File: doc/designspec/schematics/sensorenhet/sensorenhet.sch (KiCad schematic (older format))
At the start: 28 parts, among them IC1 ATMEGA1284P-P, U1 IQEXO-3, U10 MLX90609, U2 Terminator-CTRL, U3 USB-UART, U4 Lidar_Lite_v2, U5 IR-Sensor, U6 IR-Sensor, U7 IR-Sensor, U8 IR-Sensor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

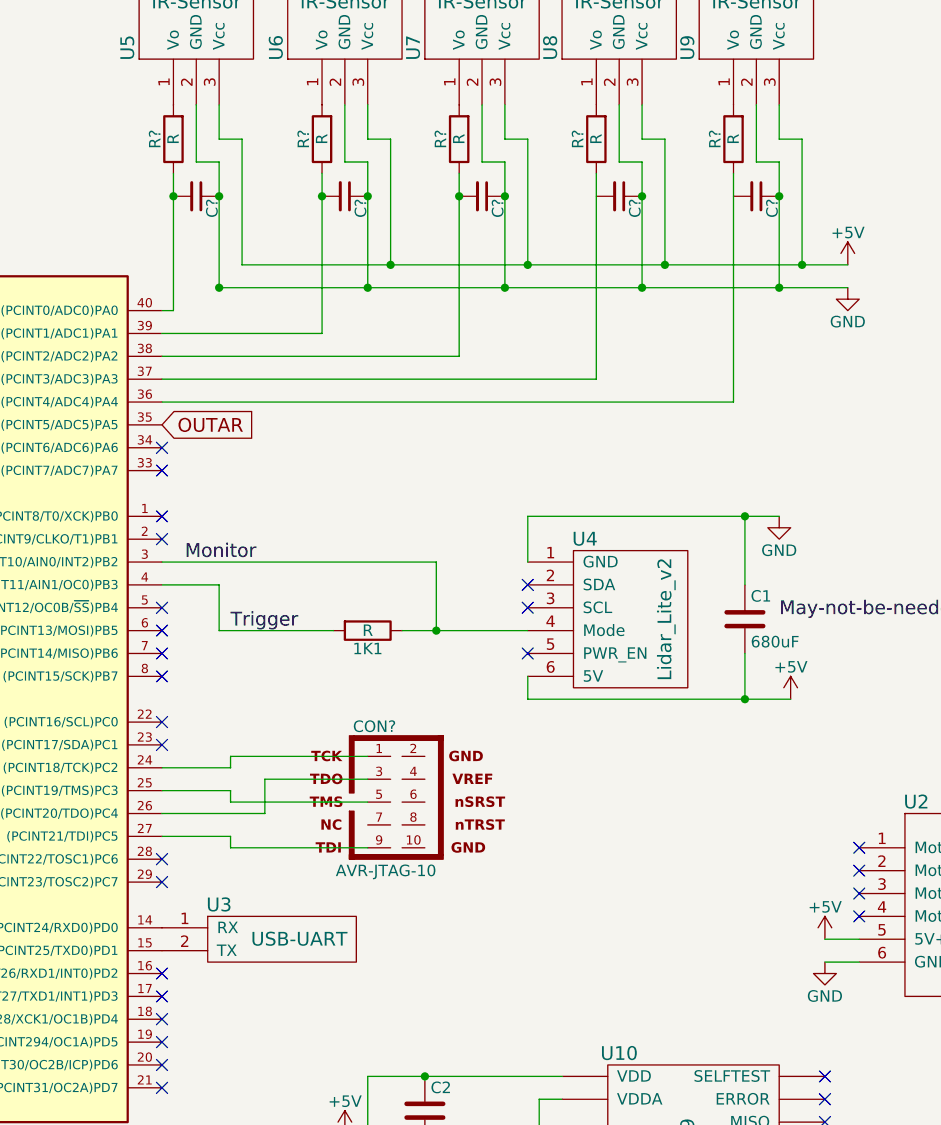
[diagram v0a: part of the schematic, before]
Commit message: Fix uart connection in kicad
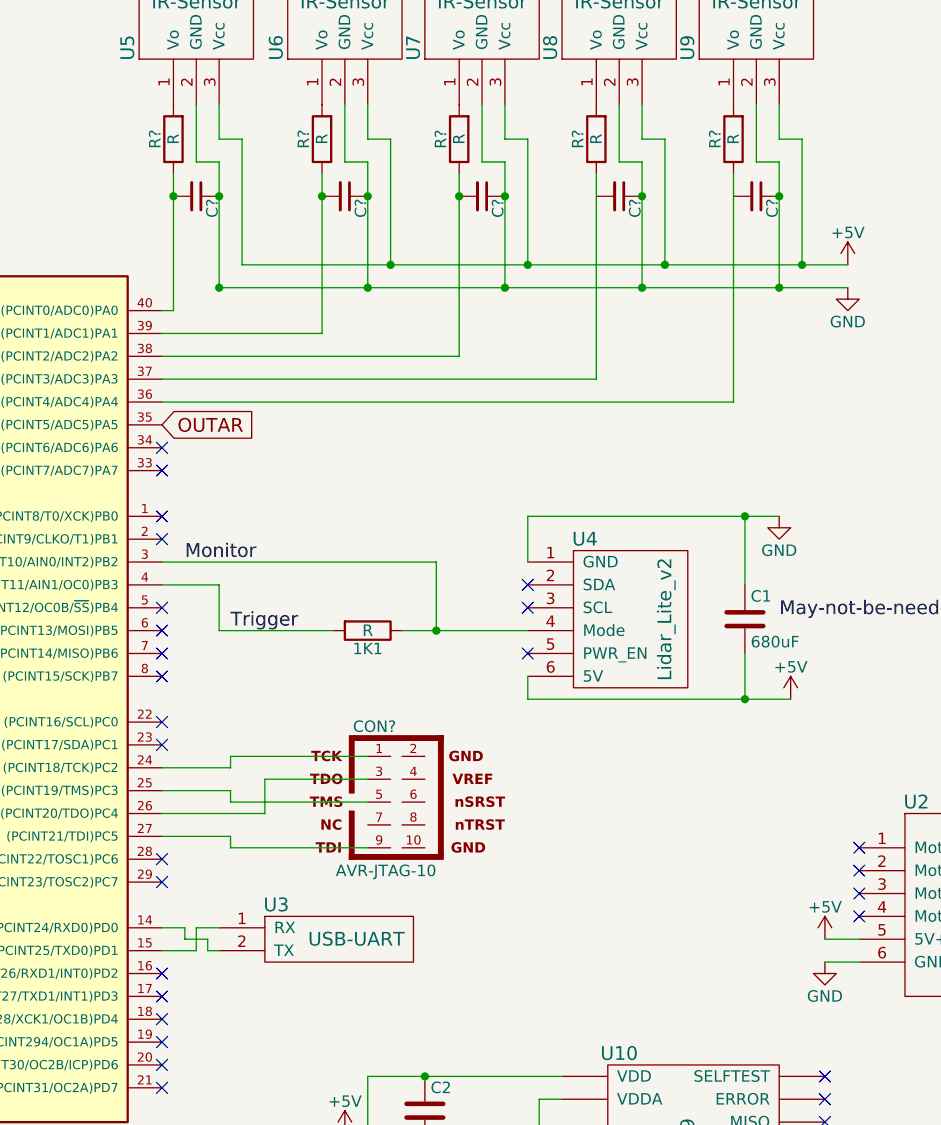
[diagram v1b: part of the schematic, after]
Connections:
- net at IC1.14 ((PCINT24/RXD0)PD0): now also U3.2 (TX); no longer U3.1 (RX)
- net at IC1.15 ((PCINT25/TXD0)PD1): now also U3.1 (RX); no longer U3.2 (TX)
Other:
- moved on the sheet: U3
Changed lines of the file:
@@
 L USB-UART U3
 U 1 1 57F7998E
-P 6350 4750
-F 0 "U3" H 6000 4900 60  0000 C CNN
-F 1 "USB-UART" H 6350 4750 60  0000 C CNN
-F 2 "" H 6350 4750 60  0001 C CNN
-F 3 "" H 6350 4750 60  0001 C CNN
-	1    6350 4750
+P 6600 4750
+F 0 "U3" H 6250 4900 60  0000 C CNN
+F 1 "USB-UART" H 6600 4750 60  0000 C CNN
+F 2 "" H 6600 4750 60  0001 C CNN
+F 3 "" H 6600 4750 60  0001 C CNN
+	1    6600 4750
 	1    0    0    -1
 $EndComp
@@
 $EndComp
 Wire Wire Line
-	7850 1900 7850 1350
+	7850 1350 7850 1900
 Wire Wire Line
 	7850 1350 7750 1350
@@
 $EndComp
 Wire Wire Line
-	8450 1900 8450 1350
+	8450 1350 8450 1900
 Wire Wire Line
 	8450 1350 8350 1350
@@
 	1    0    0    -1
 $EndComp
+Wire Wire Line
+	6000 4700 5900 4700
+Wire Wire Line
+	5900 4700 5900 4800
+Wire Wire Line
+	5900 4800 5750 4800
+Wire Wire Line
+	5750 4700 5850 4700
+Wire Wire Line
+	5850 4700 5850 4750
+Wire Wire Line
+	5850 4750 5950 4750
+Wire Wire Line
+	5950 4750 5950 4800
+Wire Wire Line
+	5950 4800 6000 4800
 $EndSCHEMATC
